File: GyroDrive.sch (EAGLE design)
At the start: 32 parts

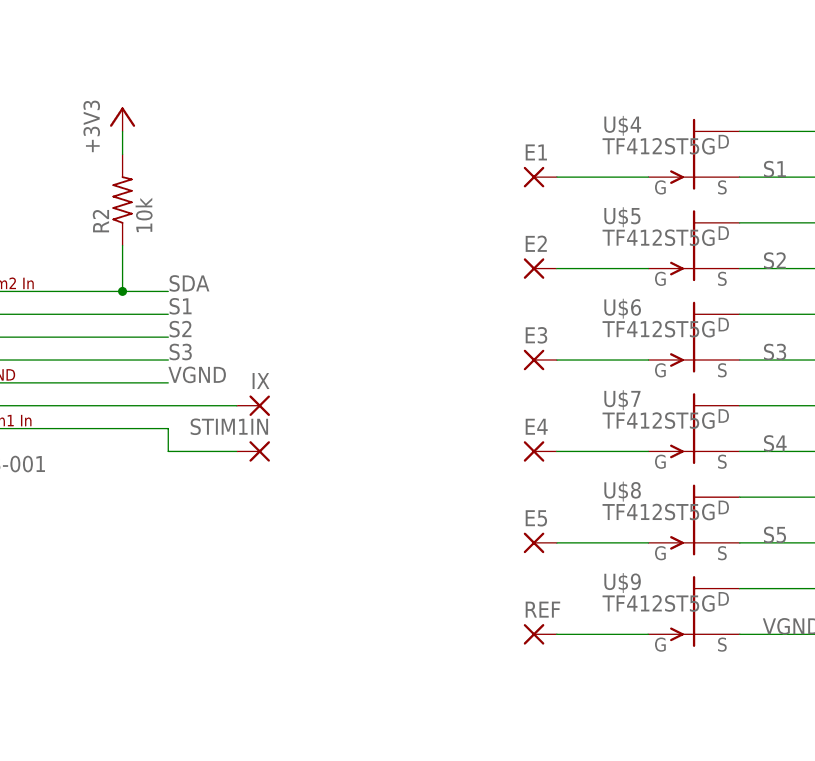
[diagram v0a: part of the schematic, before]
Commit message: Preliminary layout with smaller through-holes
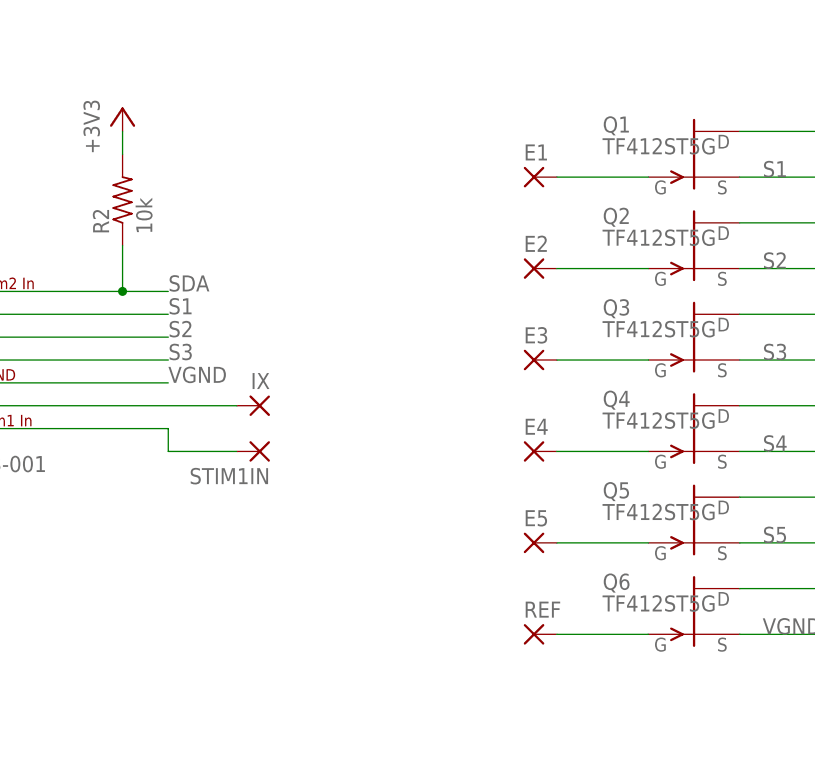
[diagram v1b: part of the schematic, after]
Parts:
- E1, E2, E3, E4, E5, GND, REF, STIM1IN, STIM1OUT: device wirepad:1,6/0,8 -> michael-stetner:THROUGH-HOLE-30MIL/15MIL
- renumbered U$4 to Q1, U$5 to Q2, U$6 to Q3, U$7 to Q4, U$8 to Q5, U$9 to Q6
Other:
- moved on the sheet: STIM1IN

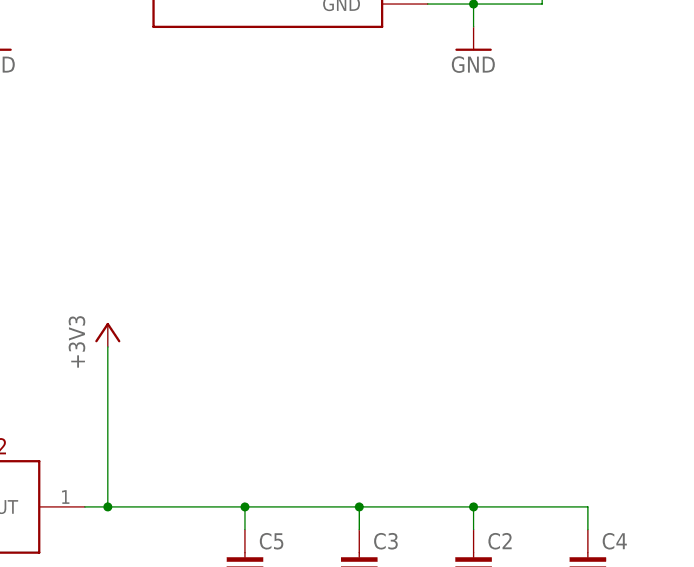
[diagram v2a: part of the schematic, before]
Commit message: Added solder jumpers for SDA, SCL, and digital ground
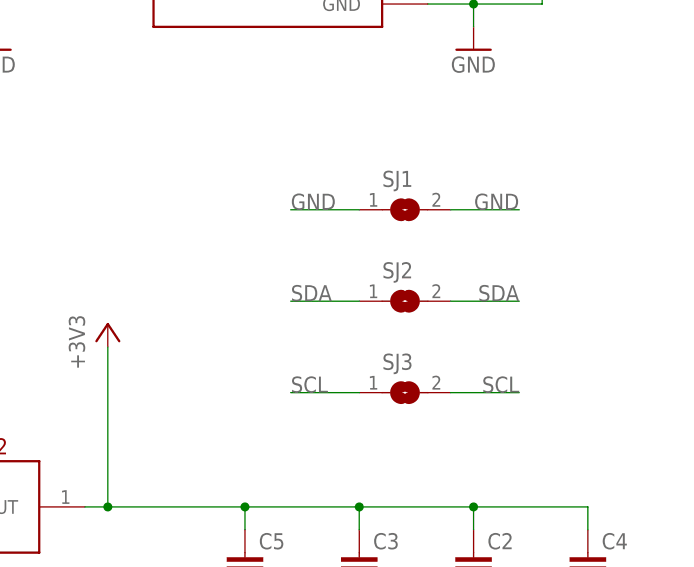
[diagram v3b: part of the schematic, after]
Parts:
- added SJ1, SJ2, SJ3: (no value), michael-stetner:SJ
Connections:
- net GND: now also SJ1.1, SJ1.2
- net SCL: now also SJ3.1, SJ3.2
- net SDA: now also SJ2.1, SJ2.2
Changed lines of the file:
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@@
 <?xml version="1.0" encoding="utf-8"?>
 <!DOCTYPE eagle SYSTEM "eagle.dtd">
-<eagle version="7.5.0">
+<eagle version="7.4.0">
 <drawing>
 <settings>
@@
 <part name="E5" library="michael-stetner" deviceset="THROUGH-HOLE-30MIL/15MIL" device=""/>
 <part name="REF" library="michael-stetner" deviceset="THROUGH-HOLE-30MIL/15MIL" device=""/>
+<part name="SJ1" library="michael-stetner" deviceset="SJ" device=""/>
+<part name="SJ2" library="michael-stetner" deviceset="SJ" device=""/>
+<part name="SJ3" library="michael-stetner" deviceset="SJ" device=""/>
 </parts>
 <sheets>
@@
 <instance part="E5" gate="P" x="114.3" y="167.64"/>
 <instance part="REF" gate="P" x="114.3" y="157.48"/>
+<instance part="SJ1" gate="1" x="137.16" y="88.9"/>
+<instance part="SJ2" gate="1" x="137.16" y="78.74"/>
+<instance part="SJ3" gate="1" x="137.16" y="68.58"/>
 </instances>
 <busses>
@@
 <junction x="5.08" y="172.72"/>
 </segment>
+<segment>
+<wire x1="132.08" y1="88.9" x2="124.46" y2="88.9" width="0.1524" layer="91"/>
+<label x="124.46" y="88.9" size="1.778" layer="95"/>
+<pinref part="SJ1" gate="1" pin="1"/>
+</segment>
+<segment>
+<wire x1="142.24" y1="88.9" x2="149.86" y2="88.9" width="0.1524" layer="91"/>
+<label x="149.86" y="88.9" size="1.778" layer="95" rot="MR0"/>
+<pinref part="SJ1" gate="1" pin="2"/>
+</segment>
 </net>
 <net name="+3V3" class="0">
@@
 <label x="12.7" y="116.84" size="1.778" layer="95"/>
 </segment>
+<segment>
+<wire x1="132.08" y1="78.74" x2="124.46" y2="78.74" width="0.1524" layer="91"/>
+<label x="124.46" y="78.74" size="1.778" layer="95"/>
+<pinref part="SJ2" gate="1" pin="1"/>
+</segment>
+<segment>
+<wire x1="142.24" y1="78.74" x2="149.86" y2="78.74" width="0.1524" layer="91"/>
+<label x="149.86" y="78.74" size="1.778" layer="95" rot="MR0"/>
+<pinref part="SJ2" gate="1" pin="2"/>
+</segment>
 </net>
 <net name="SCL" class="0">
@@
 <label x="12.7" y="119.38" size="1.778" layer="95"/>
 </segment>
+<segment>
+<wire x1="132.08" y1="68.58" x2="124.46" y2="68.58" width="0.1524" layer="91"/>
+<label x="124.46" y="68.58" size="1.778" layer="95"/>
+<pinref part="SJ3" gate="1" pin="1"/>
+</segment>
+<segment>
+<wire x1="142.24" y1="68.58" x2="149.86" y2="68.58" width="0.1524" layer="91"/>
+<label x="149.86" y="68.58" size="1.778" layer="95" rot="MR0"/>
+<pinref part="SJ3" gate="1" pin="2"/>
+</segment>
 </net>

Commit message: Silkscreen
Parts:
- renumbered SJ1 to J_GND, SJ2 to J_SDA, SJ3 to J_SCL
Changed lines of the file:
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@@
 <part name="E5" library="michael-stetner" deviceset="THROUGH-HOLE-30MIL/15MIL" device=""/>
 <part name="REF" library="michael-stetner" deviceset="THROUGH-HOLE-30MIL/15MIL" device=""/>
-<part name="SJ1" library="michael-stetner" deviceset="SJ" device=""/>
-<part name="SJ2" library="michael-stetner" deviceset="SJ" device=""/>
-<part name="SJ3" library="michael-stetner" deviceset="SJ" device=""/>
+<part name="J_GND" library="michael-stetner" deviceset="SJ" device=""/>
+<part name="J_SDA" library="michael-stetner" deviceset="SJ" device=""/>
+<part name="J_SCL" library="michael-stetner" deviceset="SJ" device=""/>
 </parts>
 <sheets>
@@
 <instance part="E5" gate="P" x="114.3" y="167.64"/>
 <instance part="REF" gate="P" x="114.3" y="157.48"/>
-<instance part="SJ1" gate="1" x="137.16" y="88.9"/>
-<instance part="SJ2" gate="1" x="137.16" y="78.74"/>
-<instance part="SJ3" gate="1" x="137.16" y="68.58"/>
+<instance part="J_GND" gate="1" x="137.16" y="88.9"/>
+<instance part="J_SDA" gate="1" x="137.16" y="78.74"/>
+<instance part="J_SCL" gate="1" x="137.16" y="68.58"/>
 </instances>
 <busses>
@@
 <wire x1="132.08" y1="88.9" x2="124.46" y2="88.9" width="0.1524" layer="91"/>
 <label x="124.46" y="88.9" size="1.778" layer="95"/>
-<pinref part="SJ1" gate="1" pin="1"/>
+<pinref part="J_GND" gate="1" pin="1"/>
 </segment>
 <segment>
 <wire x1="142.24" y1="88.9" x2="149.86" y2="88.9" width="0.1524" layer="91"/>
 <label x="149.86" y="88.9" size="1.778" layer="95" rot="MR0"/>
-<pinref part="SJ1" gate="1" pin="2"/>
+<pinref part="J_GND" gate="1" pin="2"/>
 </segment>
 </net>
@@
 <wire x1="132.08" y1="78.74" x2="124.46" y2="78.74" width="0.1524" layer="91"/>
 <label x="124.46" y="78.74" size="1.778" layer="95"/>
-<pinref part="SJ2" gate="1" pin="1"/>
+<pinref part="J_SDA" gate="1" pin="1"/>
 </segment>
 <segment>
 <wire x1="142.24" y1="78.74" x2="149.86" y2="78.74" width="0.1524" layer="91"/>
 <label x="149.86" y="78.74" size="1.778" layer="95" rot="MR0"/>
-<pinref part="SJ2" gate="1" pin="2"/>
+<pinref part="J_SDA" gate="1" pin="2"/>
 </segment>
 </net>
@@
 <wire x1="132.08" y1="68.58" x2="124.46" y2="68.58" width="0.1524" layer="91"/>
 <label x="124.46" y="68.58" size="1.778" layer="95"/>
-<pinref part="SJ3" gate="1" pin="1"/>
+<pinref part="J_SCL" gate="1" pin="1"/>
 </segment>
 <segment>
 <wire x1="142.24" y1="68.58" x2="149.86" y2="68.58" width="0.1524" layer="91"/>
 <label x="149.86" y="68.58" size="1.778" layer="95" rot="MR0"/>
-<pinref part="SJ3" gate="1" pin="2"/>
-</segment>
-</net>
+<pinref part="J_SCL" gate="1" pin="2"/>
+</segment>
+</net>

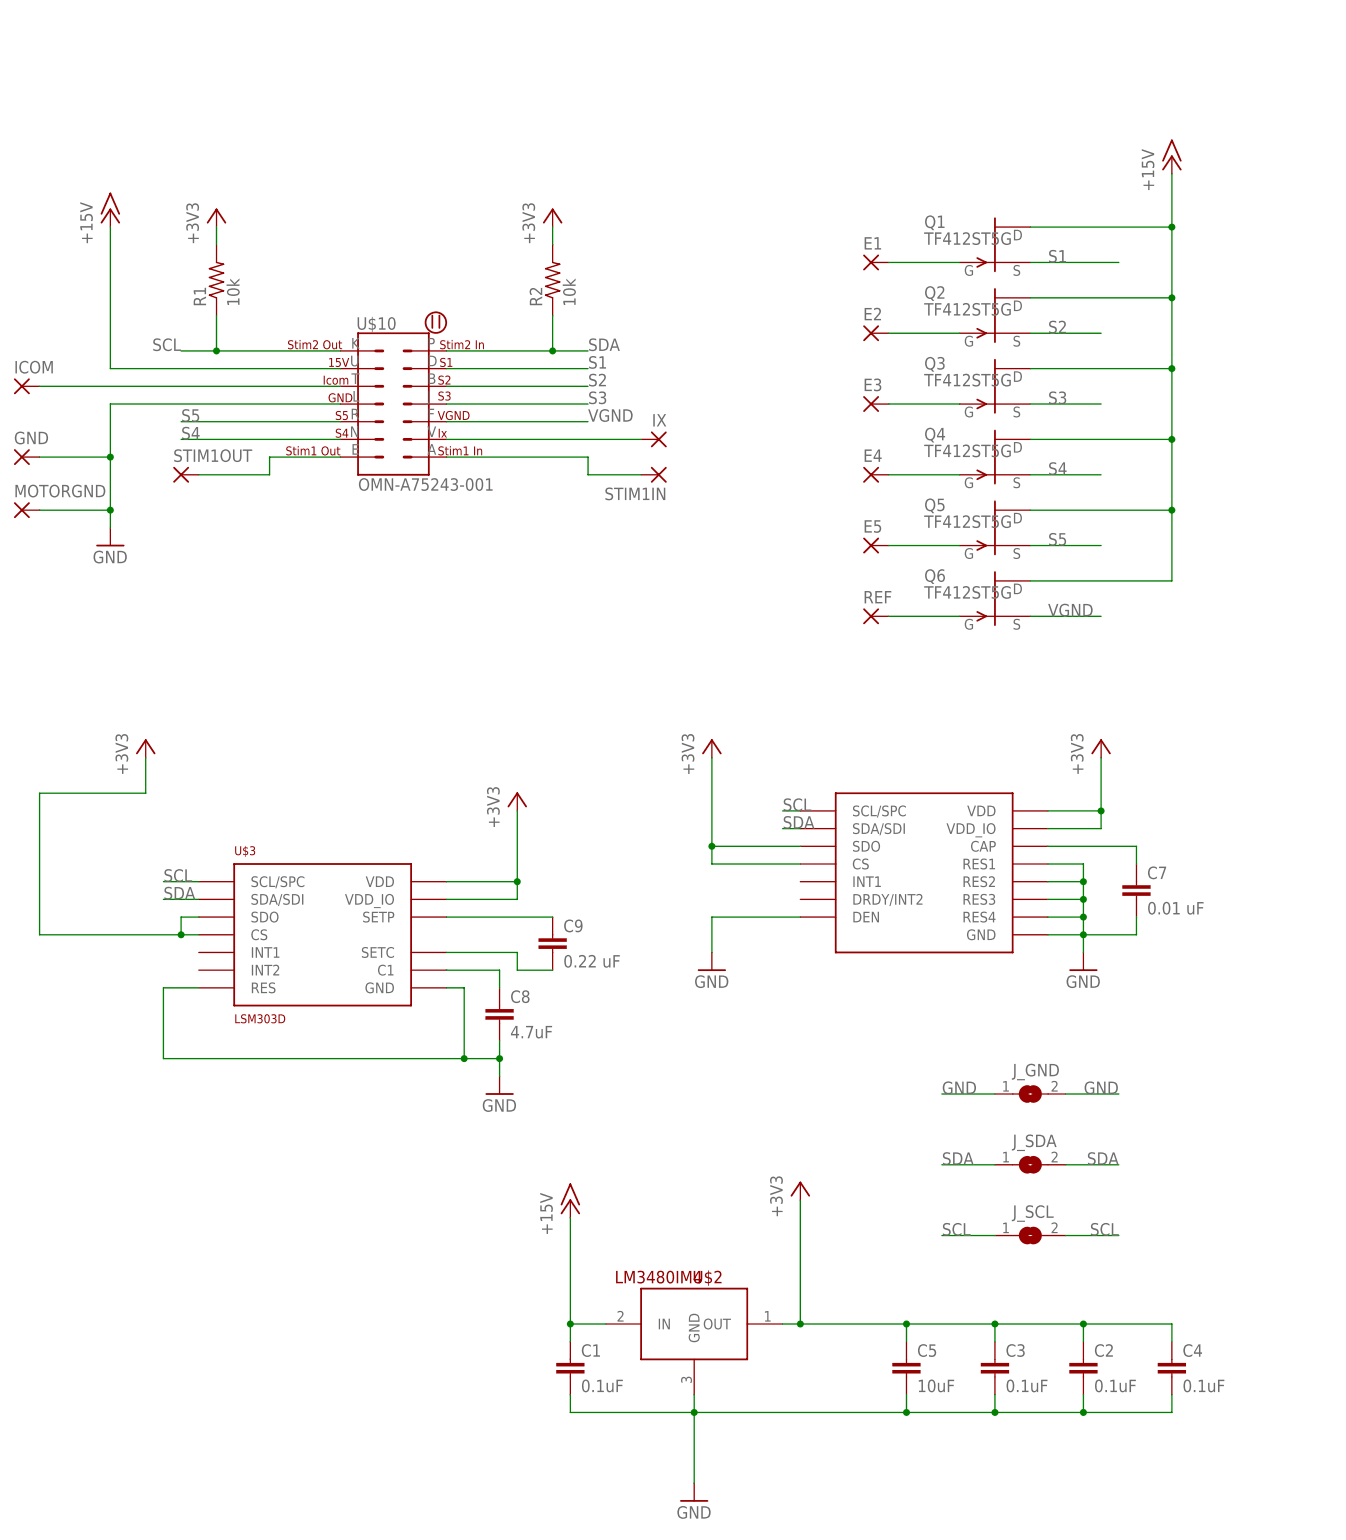
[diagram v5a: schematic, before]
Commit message: Changed schematic to make more sense (Rev 3 to Advanced Circuits)
- Changed input voltage net name from +15V to VCC because VCC can be anything from 2.5V to 30V

- Separate nets for digital and analog grounds (DGND and GND)
-- Causes DRC to catch my mistake when digital and analog ground overlap

- New nets SDAOUT and SCLOUT to represent SDA and SCL after passing through jumper
-- Stops ratsnest from telling me I have things to do when the two terminals of the jumper are not connected to each other
-- Pullup resistors moved to SDA and SCL nets (they used to be near omnetics connector on schematic, which put them on SDAOUT and SCLOUT)

- Capacitors renumbered and moved around
-- Location on schematic is now more representative of location on the board
-- Numbered so that capacitors that are associated with the same IC are sequential.
--- C1-C2 for regulator
--- C3 for big bypass capacitor
--- C4-C5 for L3GD20H
--- C6-C8 for LSM303D
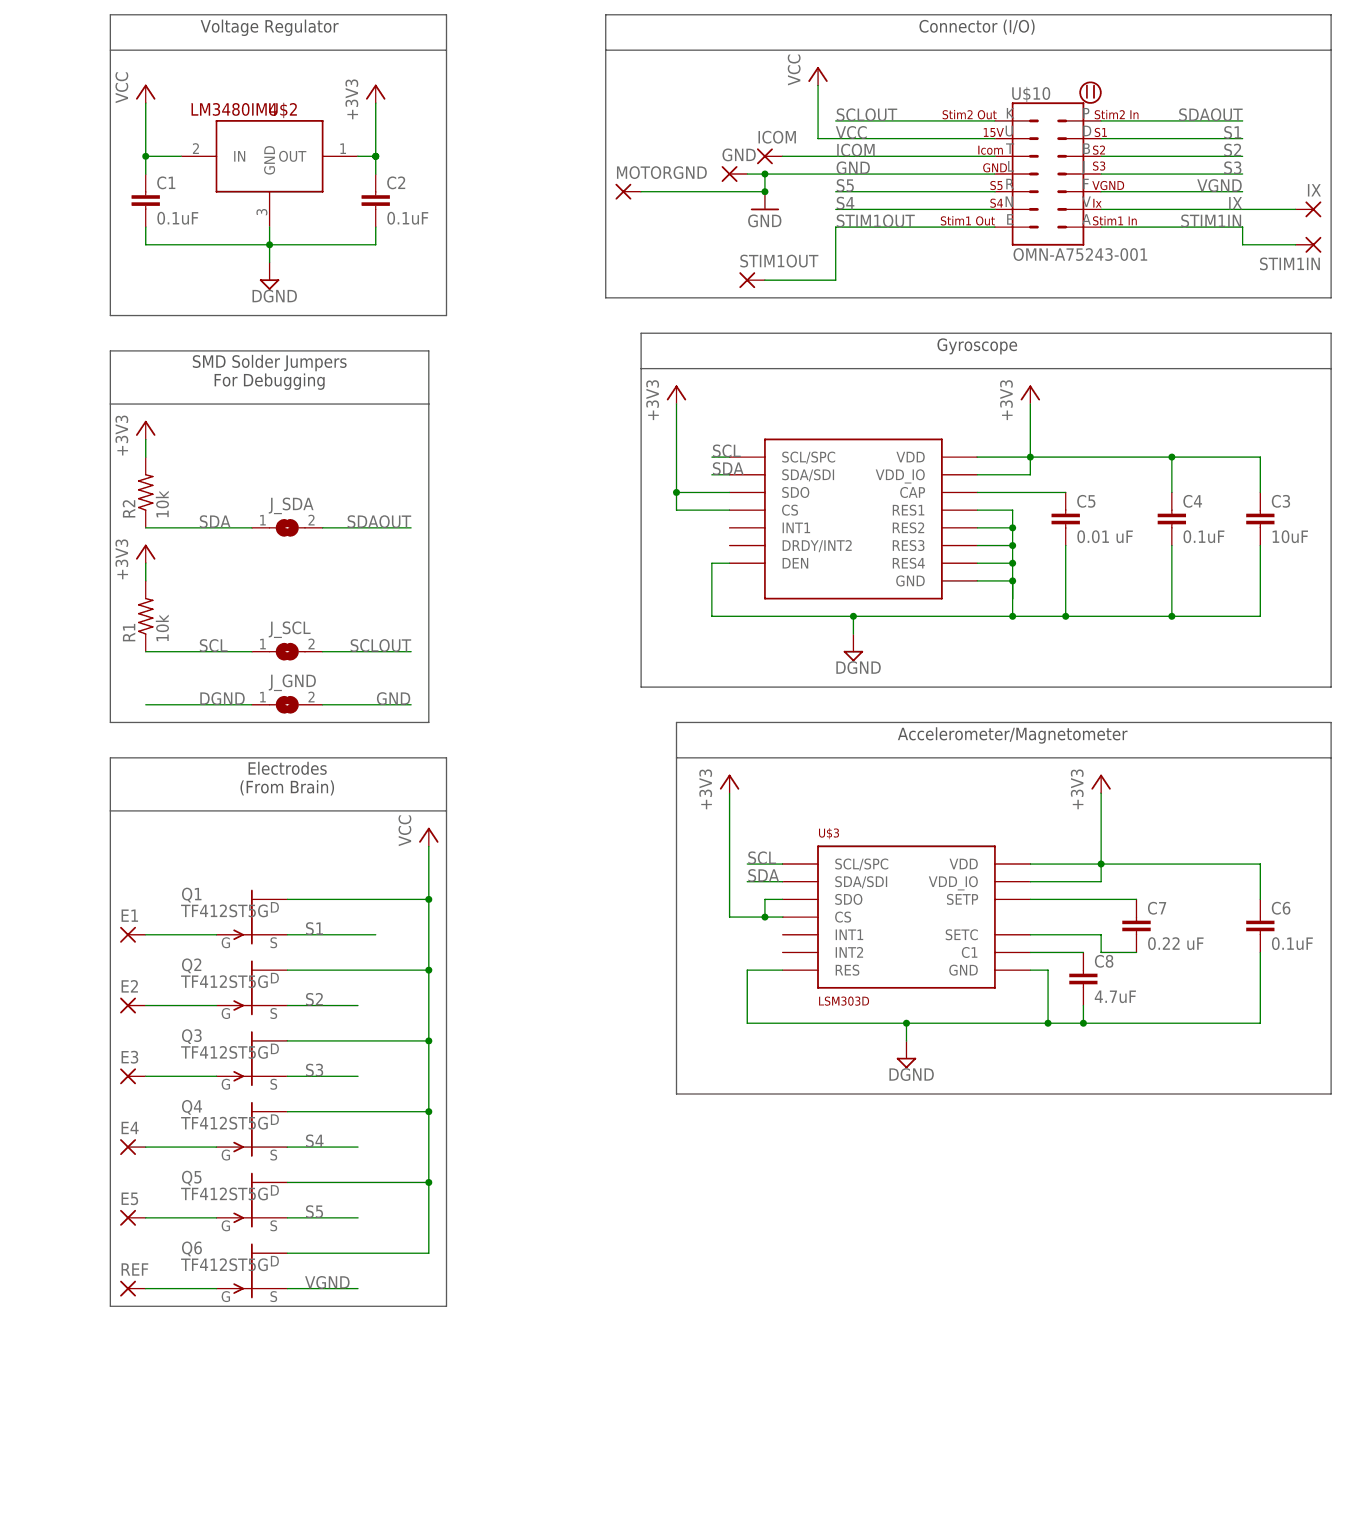
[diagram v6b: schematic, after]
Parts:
- removed C9: 0.22 uF, resistor:C-EUC0201
- added C6: 0.1uF, resistor:C-EUC0201
- C3: value 0.1uF -> 10uF; device resistor:C-EUC0201 -> resistor:C-EUC0603
- C5: value 10uF -> 0.01 uF; device resistor:C-EUC0603 -> resistor:C-EUC0402
- C7: value 0.01 uF -> 0.22 uF; device resistor:C-EUC0402 -> resistor:C-EUC0201
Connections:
- net +15V renamed VCC
- net N$11 renamed STIM1OUT
- net N$12 renamed ICOM
- net N$15 renamed IX
- net N$16 renamed STIM1IN
- new net DGND: C1.2, C2.2, C3.2, C4.2, C5.2, C6.2, C8.2, J_GND.1, U$1.DEN, U$1.GND, U$1.RES1, U$1.RES2, U$1.RES3, U$1.RES4, U$2.GND, U$3.GND, U$3.RES
- new net SCLOUT: J_SCL.2, U$10.K
- new net SDAOUT: J_SDA.2, U$10.P
- net +3V3: now also C6.1; no longer C5.1
- net GND: no longer C1.2, C2.2, C3.2, C4.2, C5.2, C7.2, C8.2, J_GND.1, U$1.DEN, U$1.GND, U$1.RES1, U$1.RES2, U$1.RES3, U$1.RES4, U$2.GND, U$3.GND, U$3.RES
- net N$2: now also C7.1; no longer C9.1
- net N$3: now also C7.2; no longer C9.2
- net N$9: now also C5.1; no longer C7.1
- net SCL: no longer J_SCL.2, U$10.K
- net SDA: no longer J_SDA.2, U$10.P
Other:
- note added: "Accelerometer/Magnetometer"
- note added: "Connector (I/O)"
- note added: "Electrodes (From Brain)"
- note added: "Gyroscope"
- note added: "SMD Solder Jumpers For Debugging"
- note added: "Voltage Regulator"
- moved on the sheet: C1, C2, C3, C4, C5, C7, C8, E1, E2, E3, E4, E5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
